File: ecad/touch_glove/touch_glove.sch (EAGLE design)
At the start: 173 parts, among them Q1 MCH3474 4A/30V, Q2 MCH3474 4A/30V, Q3 MCH3474 4A/30V, Q4 MCH3474 4A/30V, Q5 MCH3474 4A/30V, Q6 MCH3474 4A/30V, SW1 4A/28V

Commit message: Completed most of the circuitry for the ET schematic.
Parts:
- added C37, C49, C63, C64, C66, C67, C68, C69, C70, C76, C78, C80: 0.1uF/50V, _capacitors:0.1UF_SMD-0402_50V-10%
- added C61: 0.1uF/25V, _capacitors:0.1UF_SMD-0603_50V-20%
- added C62: 0.1uF/250V, _capacitors:0.1UF_SMD-0805_250V-10%
- added C65: 100uF/10V, _capacitors:100UF-POLARIZED_TANT_SMD-1206_10V-20%
- added C71, C72, C73, C75, C77, C79: 10uF/6.3V, _capacitors:10UF_CER_SMD-0402_6.3V-20%
- added C74: 4.7uF/10V/0402, _capacitors:4.7UF_CER_SMD-0402_10V-20%
- added ET_INDEX_PIXEL1-1, ET_INDEX_PIXEL1-10, ET_INDEX_PIXEL1-11, ET_INDEX_PIXEL1-12, ET_INDEX_PIXEL1-13, ET_INDEX_PIXEL1-14, ET_INDEX_PIXEL1-15, ET_INDEX_PIXEL1-16, ET_INDEX_PIXEL1-17, ET_INDEX_PIXEL1-18, ET_INDEX_PIXEL1-19, ET_INDEX_PIXEL1-2, ET_INDEX_PIXEL1-20, ET_INDEX_PIXEL1-3, ET_INDEX_PIXEL1-4, ET_INDEX_PIXEL1-5, ET_INDEX_PIXEL1-6, ET_INDEX_PIXEL1-7, ET_INDEX_PIXEL1-8, ET_INDEX_PIXEL1-9, ET_INDEX_PIXEL2-1, ET_INDEX_PIXEL2-10, ET_INDEX_PIXEL2-11, ET_INDEX_PIXEL2-12, ET_INDEX_PIXEL2-13, ET_INDEX_PIXEL2-14, ET_INDEX_PIXEL2-15, ET_INDEX_PIXEL2-16, ET_INDEX_PIXEL2-17, ET_INDEX_PIXEL2-18, ET_INDEX_PIXEL2-19, ET_INDEX_PIXEL2-2, ET_INDEX_PIXEL2-20, ET_INDEX_PIXEL2-3, ET_INDEX_PIXEL2-4, ET_INDEX_PIXEL2-5, ET_INDEX_PIXEL2-6, ET_INDEX_PIXEL2-7, ET_INDEX_PIXEL2-8, ET_INDEX_PIXEL2-9, ET_INDEX_PIXEL3-1, ET_INDEX_PIXEL3-10, ET_INDEX_PIXEL3-11, ET_INDEX_PIXEL3-12, ET_INDEX_PIXEL3-13, ET_INDEX_PIXEL3-14, ET_INDEX_PIXEL3-15, ET_INDEX_PIXEL3-16, ET_INDEX_PIXEL3-17, ET_INDEX_PIXEL3-18, ET_INDEX_PIXEL3-19, ET_INDEX_PIXEL3-2, ET_INDEX_PIXEL3-20, ET_INDEX_PIXEL3-3, ET_INDEX_PIXEL3-4, ET_INDEX_PIXEL3-5, ET_INDEX_PIXEL3-6, ET_INDEX_PIXEL3-7, ET_INDEX_PIXEL3-8, ET_INDEX_PIXEL3-9, ET_INDEX_PIXEL4-1, ET_INDEX_PIXEL4-10, ET_INDEX_PIXEL4-11, ET_INDEX_PIXEL4-12, ET_INDEX_PIXEL4-13, ET_INDEX_PIXEL4-14, ET_INDEX_PIXEL4-15, ET_INDEX_PIXEL4-16, ET_INDEX_PIXEL4-17, ET_INDEX_PIXEL4-18, ET_INDEX_PIXEL4-19, ET_INDEX_PIXEL4-2, ET_INDEX_PIXEL4-20, ET_INDEX_PIXEL4-3, ET_INDEX_PIXEL4-4, ET_INDEX_PIXEL4-5, ET_INDEX_PIXEL4-6, ET_INDEX_PIXEL4-7, ET_INDEX_PIXEL4-8, ET_INDEX_PIXEL4-9: SPST-NO 170mA 250V, _relay:RELAY_SOLID-STATE_SSR_170MA_250V_SPST-NO
- added IC1: DRV8662, _special:DRV8662_PIEZO_HAPTICS_DRIVER_QFN-20-EP
- added J1, J2, J3, J4, J5: VERT MALE 2.54MM, _connectors:1X16_PTH_VERT_MALE_2.54MM
- added J6, J7, J8, J9: PTH VERT MALE, _connectors:1X02_PTH_VERT_MALE_2.54MM
- added L3: 4.7uH/1.4A, _inductors:4.7UH_SMD-2520_1.4A-0.216OHM-20%
- added L4: 10uH/380mA, _inductors:10UH_SMD-0603_0.38A-0.468OHM-10%
- added NFET1: 2N7002DW, _transistors:MOSFET_N-CHANNEL_2-ARRAY_2N7002DW_115MA-60V
- added OPAMP4: TLV2361_GP_20MA_7MHZ, _op_amps:TLV2361_GP_20MA_7MHZ
- added POT1: 100K, _resistors:POTENTIOMETER_ST4ETB104_100K-1/4W-20%
- added PWM_DRIVER2, PWM_DRIVER3, PWM_DRIVER4, PWM_DRIVER5, PWM_DRIVER6: PCA9685, _special:PCA9685_16-CH_12-BIT_PWM-DRIVER_TSSOP-28_PWM-DRIVER_16CH
- added R100, R101, R102, R103, R104, R105, R106, R107, R108, R109, R110, R111, R112, R113, R114, R115, R116, R117, R118, R119, R120, R121, R122, R123, R124, R125, R126, R127, R128, R129, R130, R131, R132, R133, R134, R135, R49, R57, R58, R59, R60, R61, R62, R63, R64, R65, R66, R67, R68, R69, R70, R71, R72, R73, R74, R75, R76, R77, R78, R79, R80, R81, R82, R83, R84, R85, R86, R87, R88, R89, R90, R91, R92, R93, R94, R95, R96, R97, R98, R99: 1K, _resistors:1KΩ_SMD-0402_1/16W-5%
- added R136, R137, R54, R55, R56: 10K, _resistors:10KΩ_SMD-0402_1/16W-5%
- added R50: 768K, _resistors:768KΩ_SMD-0402_1/16W-1%
- added R51: 35.7K, _resistors:35.7KΩ_SMD-0402_1/16W-1%
- added R52: 20K, _resistors:20KΩ_SMD-0402_1/16W-1%
- added R53: 41.2K, _resistors:41.2KΩ_SMD-0402_1/16W-1%
- added REXT: 7.5K, _resistors:7.5KΩ_SMD-0402_1/16W-1%
- added SW2: 25mA/24V, _switches:SWITCH_SPST_ARRAY-3_SLIDE_DIP_SPST_25MA_24V
- added VREG-MCU1: TPS76833QDR 1A/3.3V, _ic_power:VREG_TPS768XX_ULDO_FAST-TRANSIENT_TPS76833QDR_1A-3.3V
- added VREG2: NCP1729 50mA, _ic_power:VREG_NCP1729_NEGATIVE_SWITCHED-CAP-INVERTER_50MA
- added VREG3: TPS62202 300mA 1.8V, _ic_power:VREG_SWITCHING_TPS6220XTPS62202_300MA_1.8V
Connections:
- new net -1.8V: C72.1, OPAMP4.V-, VREG2.VOUT
- new net C+: C71.1, VREG2.C+
- new net C-: C71.2, VREG2.C-
- new net EN: IC1.EN, R54.2, SW2.S3
- new net FB: IC1.FB, R50.1, R51.2, R52.2, R53.2
- new net GAIN0: IC1.GAIN0, NFET1.G2, R55.2, SW2.S2
- new net GAIN1: IC1.GAIN1, NFET1.G1, R56.2, SW2.S1
- new net IN+: C64.1, OPAMP4.OUT, POT1.CCW, POT1.S, R136.2
- new net INDEX_IN1-1: ET_INDEX_PIXEL1-1.1, ET_INDEX_PIXEL1-13.1, ET_INDEX_PIXEL1-17.1, ET_INDEX_PIXEL1-5.1, ET_INDEX_PIXEL1-9.1, PWM_DRIVER2.PWM0, PWM_DRIVER3.PWM0, PWM_DRIVER4.PWM0, PWM_DRIVER5.PWM0, PWM_DRIVER6.PWM0
- new net INDEX_IN1-2: ET_INDEX_PIXEL1-10.1, ET_INDEX_PIXEL1-14.1, ET_INDEX_PIXEL1-18.1, ET_INDEX_PIXEL1-2.1, ET_INDEX_PIXEL1-6.1, PWM_DRIVER2.PWM1, PWM_DRIVER3.PWM1, PWM_DRIVER4.PWM1, PWM_DRIVER5.PWM1, PWM_DRIVER6.PWM1
- new net INDEX_IN1-3: ET_INDEX_PIXEL1-11.1, ET_INDEX_PIXEL1-15.1, ET_INDEX_PIXEL1-19.1, ET_INDEX_PIXEL1-3.1, ET_INDEX_PIXEL1-7.1, PWM_DRIVER2.PWM2, PWM_DRIVER3.PWM2, PWM_DRIVER4.PWM2, PWM_DRIVER5.PWM2, PWM_DRIVER6.PWM2
- new net INDEX_IN1-4: ET_INDEX_PIXEL1-12.1, ET_INDEX_PIXEL1-16.1, ET_INDEX_PIXEL1-20.1, ET_INDEX_PIXEL1-4.1, ET_INDEX_PIXEL1-8.1, PWM_DRIVER2.PWM3, PWM_DRIVER3.PWM3, PWM_DRIVER4.PWM3, PWM_DRIVER5.PWM3, PWM_DRIVER6.PWM3
- new net INDEX_IN2-1: ET_INDEX_PIXEL2-1.1, ET_INDEX_PIXEL2-11.1, ET_INDEX_PIXEL2-15.1, ET_INDEX_PIXEL2-19.1, ET_INDEX_PIXEL2-7.1, PWM_DRIVER2.PWM4, PWM_DRIVER3.PWM4, PWM_DRIVER4.PWM4, PWM_DRIVER5.PWM4, PWM_DRIVER6.PWM4
- new net INDEX_IN2-2: ET_INDEX_PIXEL2-10.1, ET_INDEX_PIXEL2-14.1, ET_INDEX_PIXEL2-18.1, ET_INDEX_PIXEL2-2.1, ET_INDEX_PIXEL2-6.1, PWM_DRIVER2.PWM5, PWM_DRIVER3.PWM5, PWM_DRIVER4.PWM5, PWM_DRIVER5.PWM5, PWM_DRIVER6.PWM5
- new net INDEX_IN2-3: ET_INDEX_PIXEL2-13.1, ET_INDEX_PIXEL2-17.1, ET_INDEX_PIXEL2-3.1, ET_INDEX_PIXEL2-5.1, ET_INDEX_PIXEL2-9.1, PWM_DRIVER2.PWM6, PWM_DRIVER3.PWM6, PWM_DRIVER4.PWM6, PWM_DRIVER5.PWM6, PWM_DRIVER6.PWM6
- new net INDEX_IN2-4: ET_INDEX_PIXEL2-12.1, ET_INDEX_PIXEL2-16.1, ET_INDEX_PIXEL2-20.1, ET_INDEX_PIXEL2-4.1, ET_INDEX_PIXEL2-8.1, PWM_DRIVER2.PWM7, PWM_DRIVER3.PWM7, PWM_DRIVER4.PWM7, PWM_DRIVER5.PWM7, PWM_DRIVER6.PWM7
- new net INDEX_IN3-1: ET_INDEX_PIXEL3-1.1, ET_INDEX_PIXEL3-13.1, ET_INDEX_PIXEL3-17.1, ET_INDEX_PIXEL3-5.1, ET_INDEX_PIXEL3-9.1, PWM_DRIVER2.PWM8, PWM_DRIVER3.PWM8, PWM_DRIVER4.PWM8, PWM_DRIVER5.PWM8, PWM_DRIVER6.PWM8
- new net INDEX_IN3-2: ET_INDEX_PIXEL3-10.1, ET_INDEX_PIXEL3-14.1, ET_INDEX_PIXEL3-18.1, ET_INDEX_PIXEL3-2.1, ET_INDEX_PIXEL3-6.1, PWM_DRIVER2.PWM9, PWM_DRIVER3.PWM9, PWM_DRIVER4.PWM9, PWM_DRIVER5.PWM9, PWM_DRIVER6.PWM9
- new net INDEX_IN3-3: ET_INDEX_PIXEL3-11.1, ET_INDEX_PIXEL3-15.1, ET_INDEX_PIXEL3-19.1, ET_INDEX_PIXEL3-3.1, ET_INDEX_PIXEL3-7.1, PWM_DRIVER2.PWM10, PWM_DRIVER3.PWM10, PWM_DRIVER4.PWM10, PWM_DRIVER5.PWM10, PWM_DRIVER6.PWM10
- new net INDEX_IN3-4: ET_INDEX_PIXEL3-12.1, ET_INDEX_PIXEL3-16.1, ET_INDEX_PIXEL3-20.1, ET_INDEX_PIXEL3-4.1, ET_INDEX_PIXEL3-8.1, PWM_DRIVER2.PWM11, PWM_DRIVER3.PWM11, PWM_DRIVER4.PWM11, PWM_DRIVER5.PWM11, PWM_DRIVER6.PWM11
- new net INDEX_IN4-1: ET_INDEX_PIXEL4-1.1, ET_INDEX_PIXEL4-13.1, ET_INDEX_PIXEL4-17.1, ET_INDEX_PIXEL4-5.1, ET_INDEX_PIXEL4-9.1, PWM_DRIVER2.PWM12, PWM_DRIVER3.PWM12, PWM_DRIVER4.PWM12, PWM_DRIVER5.PWM12, PWM_DRIVER6.PWM12
- new net INDEX_IN4-2: ET_INDEX_PIXEL4-10.1, ET_INDEX_PIXEL4-14.1, ET_INDEX_PIXEL4-18.1, ET_INDEX_PIXEL4-2.1, ET_INDEX_PIXEL4-6.1, PWM_DRIVER2.PWM13, PWM_DRIVER3.PWM13, PWM_DRIVER4.PWM13, PWM_DRIVER5.PWM13, PWM_DRIVER6.PWM13
- new net INDEX_IN4-3: ET_INDEX_PIXEL4-11.1, ET_INDEX_PIXEL4-15.1, ET_INDEX_PIXEL4-19.1, ET_INDEX_PIXEL4-3.1, ET_INDEX_PIXEL4-7.1, PWM_DRIVER2.PWM14, PWM_DRIVER3.PWM14, PWM_DRIVER4.PWM14, PWM_DRIVER5.PWM14, PWM_DRIVER6.PWM14
- new net INDEX_IN4-4: ET_INDEX_PIXEL4-12.1, ET_INDEX_PIXEL4-16.1, ET_INDEX_PIXEL4-20.1, ET_INDEX_PIXEL4-4.1, ET_INDEX_PIXEL4-8.1, PWM_DRIVER2.PWM15, PWM_DRIVER3.PWM15, PWM_DRIVER4.PWM15, PWM_DRIVER5.PWM15, PWM_DRIVER6.PWM15
- new net INDEX_OUT1-1: ET_INDEX_PIXEL1-1.3, ET_INDEX_PIXEL1-13.3, ET_INDEX_PIXEL1-17.3, ET_INDEX_PIXEL1-5.3, ET_INDEX_PIXEL1-9.3, J1.1, J2.1, J3.1, J4.1, J5.1
- new net INDEX_OUT1-2: ET_INDEX_PIXEL1-10.3, ET_INDEX_PIXEL1-14.3, ET_INDEX_PIXEL1-18.3, ET_INDEX_PIXEL1-2.3, ET_INDEX_PIXEL1-6.3
- new net INDEX_OUT1-3: ET_INDEX_PIXEL1-11.3, ET_INDEX_PIXEL1-15.3, ET_INDEX_PIXEL1-19.3, ET_INDEX_PIXEL1-3.3, ET_INDEX_PIXEL1-7.3
- new net INDEX_OUT1-4: ET_INDEX_PIXEL1-12.3, ET_INDEX_PIXEL1-16.3, ET_INDEX_PIXEL1-20.3, ET_INDEX_PIXEL1-4.3, ET_INDEX_PIXEL1-8.3
- new net INDEX_OUT2-1: ET_INDEX_PIXEL2-1.3, ET_INDEX_PIXEL2-11.3, ET_INDEX_PIXEL2-15.3, ET_INDEX_PIXEL2-19.3, ET_INDEX_PIXEL2-7.3
- new net INDEX_OUT2-2: ET_INDEX_PIXEL2-10.3, ET_INDEX_PIXEL2-14.3, ET_INDEX_PIXEL2-18.3, ET_INDEX_PIXEL2-2.3, ET_INDEX_PIXEL2-6.3
- new net INDEX_OUT2-3: ET_INDEX_PIXEL2-13.3, ET_INDEX_PIXEL2-17.3, ET_INDEX_PIXEL2-3.3, ET_INDEX_PIXEL2-5.3, ET_INDEX_PIXEL2-9.3
- new net INDEX_OUT2-4: ET_INDEX_PIXEL2-12.3, ET_INDEX_PIXEL2-16.3, ET_INDEX_PIXEL2-20.3, ET_INDEX_PIXEL2-4.3, ET_INDEX_PIXEL2-8.3
- new net INDEX_OUT3-1: ET_INDEX_PIXEL3-1.3, ET_INDEX_PIXEL3-13.3, ET_INDEX_PIXEL3-17.3, ET_INDEX_PIXEL3-5.3, ET_INDEX_PIXEL3-9.3
- new net INDEX_OUT3-2: ET_INDEX_PIXEL3-10.3, ET_INDEX_PIXEL3-14.3, ET_INDEX_PIXEL3-18.3, ET_INDEX_PIXEL3-2.3, ET_INDEX_PIXEL3-6.3
- new net INDEX_OUT3-3: ET_INDEX_PIXEL3-11.3, ET_INDEX_PIXEL3-15.3, ET_INDEX_PIXEL3-19.3, ET_INDEX_PIXEL3-3.3, ET_INDEX_PIXEL3-7.3
- new net INDEX_OUT3-4: ET_INDEX_PIXEL3-12.3, ET_INDEX_PIXEL3-16.3, ET_INDEX_PIXEL3-20.3, ET_INDEX_PIXEL3-4.3, ET_INDEX_PIXEL3-8.3
- new net INDEX_OUT4-1: ET_INDEX_PIXEL4-1.3, ET_INDEX_PIXEL4-13.3, ET_INDEX_PIXEL4-17.3, ET_INDEX_PIXEL4-5.3, ET_INDEX_PIXEL4-9.3
- new net INDEX_OUT4-2: ET_INDEX_PIXEL4-10.3, ET_INDEX_PIXEL4-14.3, ET_INDEX_PIXEL4-18.3, ET_INDEX_PIXEL4-2.3, ET_INDEX_PIXEL4-6.3
- new net INDEX_OUT4-3: ET_INDEX_PIXEL4-11.3, ET_INDEX_PIXEL4-15.3, ET_INDEX_PIXEL4-19.3, ET_INDEX_PIXEL4-3.3, ET_INDEX_PIXEL4-7.3
- new net INDEX_OUT4-4: ET_INDEX_PIXEL4-12.3, ET_INDEX_PIXEL4-16.3, ET_INDEX_PIXEL4-20.3, ET_INDEX_PIXEL4-4.3, ET_INDEX_PIXEL4-8.3
- new net N$100: ET_INDEX_PIXEL3-12.2, R99.2
- new net N$101: ET_INDEX_PIXEL4-9.2, R100.2
- new net N$102: ET_INDEX_PIXEL4-10.2, R101.2
- new net N$103: ET_INDEX_PIXEL4-11.2, R102.2
- new net N$104: ET_INDEX_PIXEL4-12.2, R103.2
- new net N$105: ET_INDEX_PIXEL1-13.2, R104.2
- new net N$106: ET_INDEX_PIXEL1-14.2, R105.2
- new net N$107: ET_INDEX_PIXEL1-15.2, R106.2
- new net N$108: ET_INDEX_PIXEL1-16.2, R107.2
- new net N$109: ET_INDEX_PIXEL2-15.2, R108.2
- new net N$110: ET_INDEX_PIXEL2-14.2, R109.2
- new net N$111: ET_INDEX_PIXEL2-13.2, R110.2
- new net N$112: ET_INDEX_PIXEL2-16.2, R111.2
- new net N$113: ET_INDEX_PIXEL3-13.2, R112.2
- new net N$114: ET_INDEX_PIXEL3-14.2, R113.2
- new net N$115: ET_INDEX_PIXEL3-15.2, R114.2
- new net N$116: ET_INDEX_PIXEL3-16.2, R115.2
- new net N$117: ET_INDEX_PIXEL4-13.2, R116.2
- new net N$118: ET_INDEX_PIXEL4-14.2, R117.2
- new net N$119: ET_INDEX_PIXEL4-15.2, R118.2
- new net N$120: ET_INDEX_PIXEL4-16.2, R119.2
- new net N$121: ET_INDEX_PIXEL1-17.2, R120.2
- new net N$122: ET_INDEX_PIXEL1-18.2, R121.2
- new net N$123: ET_INDEX_PIXEL1-19.2, R122.2
- new net N$124: ET_INDEX_PIXEL1-20.2, R123.2
- new net N$125: ET_INDEX_PIXEL2-19.2, R124.2
- new net N$126: ET_INDEX_PIXEL2-18.2, R125.2
- new net N$127: ET_INDEX_PIXEL2-17.2, R126.2
- new net N$128: ET_INDEX_PIXEL2-20.2, R127.2
- new net N$129: ET_INDEX_PIXEL3-17.2, R128.2
- new net N$130: ET_INDEX_PIXEL3-18.2, R129.2
- new net N$131: ET_INDEX_PIXEL3-19.2, R130.2
- new net N$132: ET_INDEX_PIXEL3-20.2, R131.2
- new net N$133: ET_INDEX_PIXEL4-17.2, R132.2
- new net N$134: ET_INDEX_PIXEL4-18.2, R133.2
- new net N$135: ET_INDEX_PIXEL4-19.2, R134.2
- new net N$136: ET_INDEX_PIXEL4-20.2, R135.2
- new net N$137: L4.1, VREG3.VOUT
- new net N$138: OPAMP4.IN+, R136.1, R137.2
- new net N$139: C76.1, OPAMP4.IN-, POT1.CW
- new net N$33: ET_INDEX_PIXEL1-3.2, R58.2
- new net N$39: ET_INDEX_PIXEL1-1.2, R49.2
- new net N$42: IC1.SW, L3.1
- new net N$43: C49.1, IC1.VPUMP
- new net N$44: C62.1, IC1.PVDD, IC1.VBST, R50.2
- new net N$48: IC1.REXT, REXT.2
- new net N$49: NFET1.D1, R52.1
- new net N$51: NFET1.D2, R53.1
- new net N$52: C64.2, IC1.IN+
- new net N$56: C63.2, IC1.IN-
- new net N$57: ET_INDEX_PIXEL1-2.2, R57.2
- new net N$58: ET_INDEX_PIXEL1-5.2, R72.2
- new net N$59: ET_INDEX_PIXEL1-4.2, R59.2
- new net N$60: ET_INDEX_PIXEL2-1.2, R60.2
- new net N$61: ET_INDEX_PIXEL2-2.2, R61.2
- new net N$64: ET_INDEX_PIXEL2-3.2, R62.2
- new net N$65: ET_INDEX_PIXEL2-4.2, R63.2
- new net N$66: ET_INDEX_PIXEL3-1.2, R64.2
- new net N$67: ET_INDEX_PIXEL3-2.2, R65.2
- new net N$68: ET_INDEX_PIXEL3-3.2, R66.2
- new net N$69: ET_INDEX_PIXEL3-4.2, R67.2
- new net N$70: ET_INDEX_PIXEL4-1.2, R68.2
- new net N$71: ET_INDEX_PIXEL4-2.2, R69.2
- new net N$72: ET_INDEX_PIXEL4-3.2, R70.2
- new net N$73: ET_INDEX_PIXEL4-4.2, R71.2
- new net N$74: ET_INDEX_PIXEL1-6.2, R73.2
- new net N$75: ET_INDEX_PIXEL1-7.2, R74.2
- new net N$76: ET_INDEX_PIXEL1-8.2, R75.2
- new net N$77: ET_INDEX_PIXEL2-7.2, R76.2
- new net N$78: ET_INDEX_PIXEL2-6.2, R77.2
- new net N$79: ET_INDEX_PIXEL2-5.2, R78.2
- new net N$80: ET_INDEX_PIXEL2-8.2, R79.2
- new net N$81: ET_INDEX_PIXEL3-5.2, R80.2
- new net N$82: ET_INDEX_PIXEL3-6.2, R81.2
- new net N$83: ET_INDEX_PIXEL3-7.2, R82.2
- new net N$84: ET_INDEX_PIXEL3-8.2, R83.2
- new net N$85: ET_INDEX_PIXEL4-5.2, R84.2
- new net N$86: ET_INDEX_PIXEL4-6.2, R85.2
- new net N$87: ET_INDEX_PIXEL4-7.2, R86.2
- new net N$88: ET_INDEX_PIXEL4-8.2, R87.2
- new net N$89: ET_INDEX_PIXEL1-9.2, R88.2
- new net N$90: ET_INDEX_PIXEL1-10.2, R89.2
- new net N$91: ET_INDEX_PIXEL1-11.2, R90.2
- new net N$92: ET_INDEX_PIXEL1-12.2, R91.2
- new net N$93: ET_INDEX_PIXEL2-11.2, R92.2
- new net N$94: ET_INDEX_PIXEL2-10.2, R93.2
- new net N$95: ET_INDEX_PIXEL2-9.2, R94.2
- new net N$96: ET_INDEX_PIXEL2-12.2, R95.2
- new net N$97: ET_INDEX_PIXEL3-9.2, R96.2
- new net N$98: ET_INDEX_PIXEL3-10.2, R97.2
- new net N$99: ET_INDEX_PIXEL3-11.2, R98.2
- new net V+: ET_INDEX_PIXEL1-1.4, ET_INDEX_PIXEL1-10.4, ET_INDEX_PIXEL1-11.4, ET_INDEX_PIXEL1-12.4, ET_INDEX_PIXEL1-13.4, ET_INDEX_PIXEL1-14.4, ET_INDEX_PIXEL1-15.4, ET_INDEX_PIXEL1-16.4, ET_INDEX_PIXEL1-17.4, ET_INDEX_PIXEL1-18.4, ET_INDEX_PIXEL1-19.4, ET_INDEX_PIXEL1-2.4, ET_INDEX_PIXEL1-20.4, ET_INDEX_PIXEL1-3.4, ET_INDEX_PIXEL1-4.4, ET_INDEX_PIXEL1-5.4, ET_INDEX_PIXEL1-6.4, ET_INDEX_PIXEL1-7.4, ET_INDEX_PIXEL1-8.4, ET_INDEX_PIXEL1-9.4, ET_INDEX_PIXEL2-1.4, ET_INDEX_PIXEL2-10.4, ET_INDEX_PIXEL2-11.4, ET_INDEX_PIXEL2-12.4, ET_INDEX_PIXEL2-13.4, ET_INDEX_PIXEL2-14.4, ET_INDEX_PIXEL2-15.4, ET_INDEX_PIXEL2-16.4, ET_INDEX_PIXEL2-17.4, ET_INDEX_PIXEL2-18.4, ET_INDEX_PIXEL2-19.4, ET_INDEX_PIXEL2-2.4, ET_INDEX_PIXEL2-20.4, ET_INDEX_PIXEL2-3.4, ET_INDEX_PIXEL2-4.4, ET_INDEX_PIXEL2-5.4, ET_INDEX_PIXEL2-6.4, ET_INDEX_PIXEL2-7.4, ET_INDEX_PIXEL2-8.4, ET_INDEX_PIXEL2-9.4, ET_INDEX_PIXEL3-1.4, ET_INDEX_PIXEL3-10.4, ET_INDEX_PIXEL3-11.4, ET_INDEX_PIXEL3-12.4, ET_INDEX_PIXEL3-13.4, ET_INDEX_PIXEL3-14.4, ET_INDEX_PIXEL3-15.4, ET_INDEX_PIXEL3-16.4, ET_INDEX_PIXEL3-17.4, ET_INDEX_PIXEL3-18.4, ET_INDEX_PIXEL3-19.4, ET_INDEX_PIXEL3-2.4, ET_INDEX_PIXEL3-20.4, ET_INDEX_PIXEL3-3.4, ET_INDEX_PIXEL3-4.4, ET_INDEX_PIXEL3-5.4, ET_INDEX_PIXEL3-6.4, ET_INDEX_PIXEL3-7.4, ET_INDEX_PIXEL3-8.4, ET_INDEX_PIXEL3-9.4, ET_INDEX_PIXEL4-1.4, ET_INDEX_PIXEL4-10.4, ET_INDEX_PIXEL4-11.4, ET_INDEX_PIXEL4-12.4, ET_INDEX_PIXEL4-13.4, ET_INDEX_PIXEL4-14.4, ET_INDEX_PIXEL4-15.4, ET_INDEX_PIXEL4-16.4, ET_INDEX_PIXEL4-17.4, ET_INDEX_PIXEL4-18.4, ET_INDEX_PIXEL4-19.4, ET_INDEX_PIXEL4-2.4, ET_INDEX_PIXEL4-20.4, ET_INDEX_PIXEL4-3.4, ET_INDEX_PIXEL4-4.4, ET_INDEX_PIXEL4-5.4, ET_INDEX_PIXEL4-6.4, ET_INDEX_PIXEL4-7.4, ET_INDEX_PIXEL4-8.4, ET_INDEX_PIXEL4-9.4, IC1.OUT+
- new net V-: IC1.OUT-, J1.16, J2.16, J3.16, J4.16, J5.16
- net 1.8V: now also C73.1, C75.1, L4.2, OPAMP4.V+, VREG2.!SHDN, VREG2.VIN, VREG3.NC/FB
- net 3.3V: now also C37.1, C61.1, C65.A, C74.1, C77.1, C78.1, IC1.VDD, L3.2, SW2.P1, SW2.P2, SW2.P3, VREG-MCU1.VOUT, VREG3.VIN
- net GND: now also C37.2, C49.2, C61.2, C62.2, C63.1, C65.K, C66.2, C67.2, C68.2, C69.2, C70.2, C72.2, C73.2, C74.2, C75.2, C76.2, C77.2, C78.2, C79.2, C80.2, IC1.GND, NFET1.S1, NFET1.S2, PWM_DRIVER2.!OE, PWM_DRIVER2.A0, PWM_DRIVER2.A1, PWM_DRIVER2.A2, PWM_DRIVER2.A3, PWM_DRIVER2.A4, PWM_DRIVER2.A5, PWM_DRIVER2.EXTCLK, PWM_DRIVER2.GND, PWM_DRIVER3.!OE, PWM_DRIVER3.A0, PWM_DRIVER3.A1, PWM_DRIVER3.A2, PWM_DRIVER3.A3, PWM_DRIVER3.A4, PWM_DRIVER3.A5, PWM_DRIVER3.EXTCLK, PWM_DRIVER3.GND, PWM_DRIVER4.!OE, PWM_DRIVER4.A0, PWM_DRIVER4.A1, PWM_DRIVER4.A2, PWM_DRIVER4.A3, PWM_DRIVER4.A4, PWM_DRIVER4.A5, PWM_DRIVER4.EXTCLK, PWM_DRIVER4.GND, PWM_DRIVER5.!OE, PWM_DRIVER5.A0, PWM_DRIVER5.A1, PWM_DRIVER5.A2, PWM_DRIVER5.A3, PWM_DRIVER5.A4, PWM_DRIVER5.A5, PWM_DRIVER5.EXTCLK, PWM_DRIVER5.GND, PWM_DRIVER6.!OE, PWM_DRIVER6.A0, PWM_DRIVER6.A1, PWM_DRIVER6.A2, PWM_DRIVER6.A3, PWM_DRIVER6.A4, PWM_DRIVER6.A5, PWM_DRIVER6.EXTCLK, PWM_DRIVER6.GND, R100.1, R101.1, R102.1, R103.1, R104.1, R105.1, R106.1, R107.1, R108.1, R109.1, R110.1, R111.1, R112.1, R113.1, R114.1, R115.1, R116.1, R117.1, R118.1, R119.1, R120.1, R121.1, R122.1, R123.1, R124.1, R125.1, R126.1, R127.1, R128.1, R129.1, R130.1, R131.1, R132.1, R133.1, R134.1, R135.1, R137.1, R49.1, R51.1, R54.1, R55.1, R56.1, R57.1, R58.1, R59.1, R60.1, R61.1, R62.1, R63.1, R64.1, R65.1, R66.1, R67.1, R68.1, R69.1, R70.1, R71.1, R72.1, R73.1, R74.1, R75.1, R76.1, R77.1, R78.1, R79.1, R80.1, R81.1, R82.1, R83.1, R84.1, R85.1, R86.1, R87.1, R88.1, R89.1, R90.1, R91.1, R92.1, R93.1, R94.1, R95.1, R96.1, R97.1, R98.1, R99.1, REXT.1, VREG-MCU1.!EN, VREG-MCU1.GND, VREG2.GND, VREG3.GND
- net N$7: now also VREG3.EN
- net SCL: now also PWM_DRIVER2.SCL, PWM_DRIVER3.SCL, PWM_DRIVER4.SCL, PWM_DRIVER5.SCL, PWM_DRIVER6.SCL
- net SDA: now also PWM_DRIVER2.SDA, PWM_DRIVER3.SDA, PWM_DRIVER4.SDA, PWM_DRIVER5.SDA, PWM_DRIVER6.SDA
- net VBAT: now also C79.1, C80.1, VREG-MCU1.VIN
- net VCC: now also C66.1, C67.1, C68.1, C69.1, C70.1, PWM_DRIVER2.VCC, PWM_DRIVER3.VCC, PWM_DRIVER4.VCC, PWM_DRIVER5.VCC, PWM_DRIVER6.VCC
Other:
- note added: "ANALOG VOLTAGE AMPLIFIER"
- note added: "ELECTROTACTILE ARRAYS"
- note added: "ET ARRAY - INDEX"
- note added: "ET ARRAY - MIDDLE"
- note added: "ET ARRAY - PINKY"
- note added: "ET ARRAY - RING"
- note added: "ET ARRAY - THUMB"
- note added: "SQW GENERATOR"
- note added: "STAGE1"
- note added: "STAGE2"
- note added: "STAGE3"
- note added: "TODO: CHECK VALUES (C1, POT1, R2,R3) AND VOLTAGE DIVIDER TO MAKE 1.8V"
- note added: "TODO: Change I2C addr"
- note added: "TODO: NAME ENABLE PIN"
- note added: "Transfer: VBAT, SDA, SCL, GND"

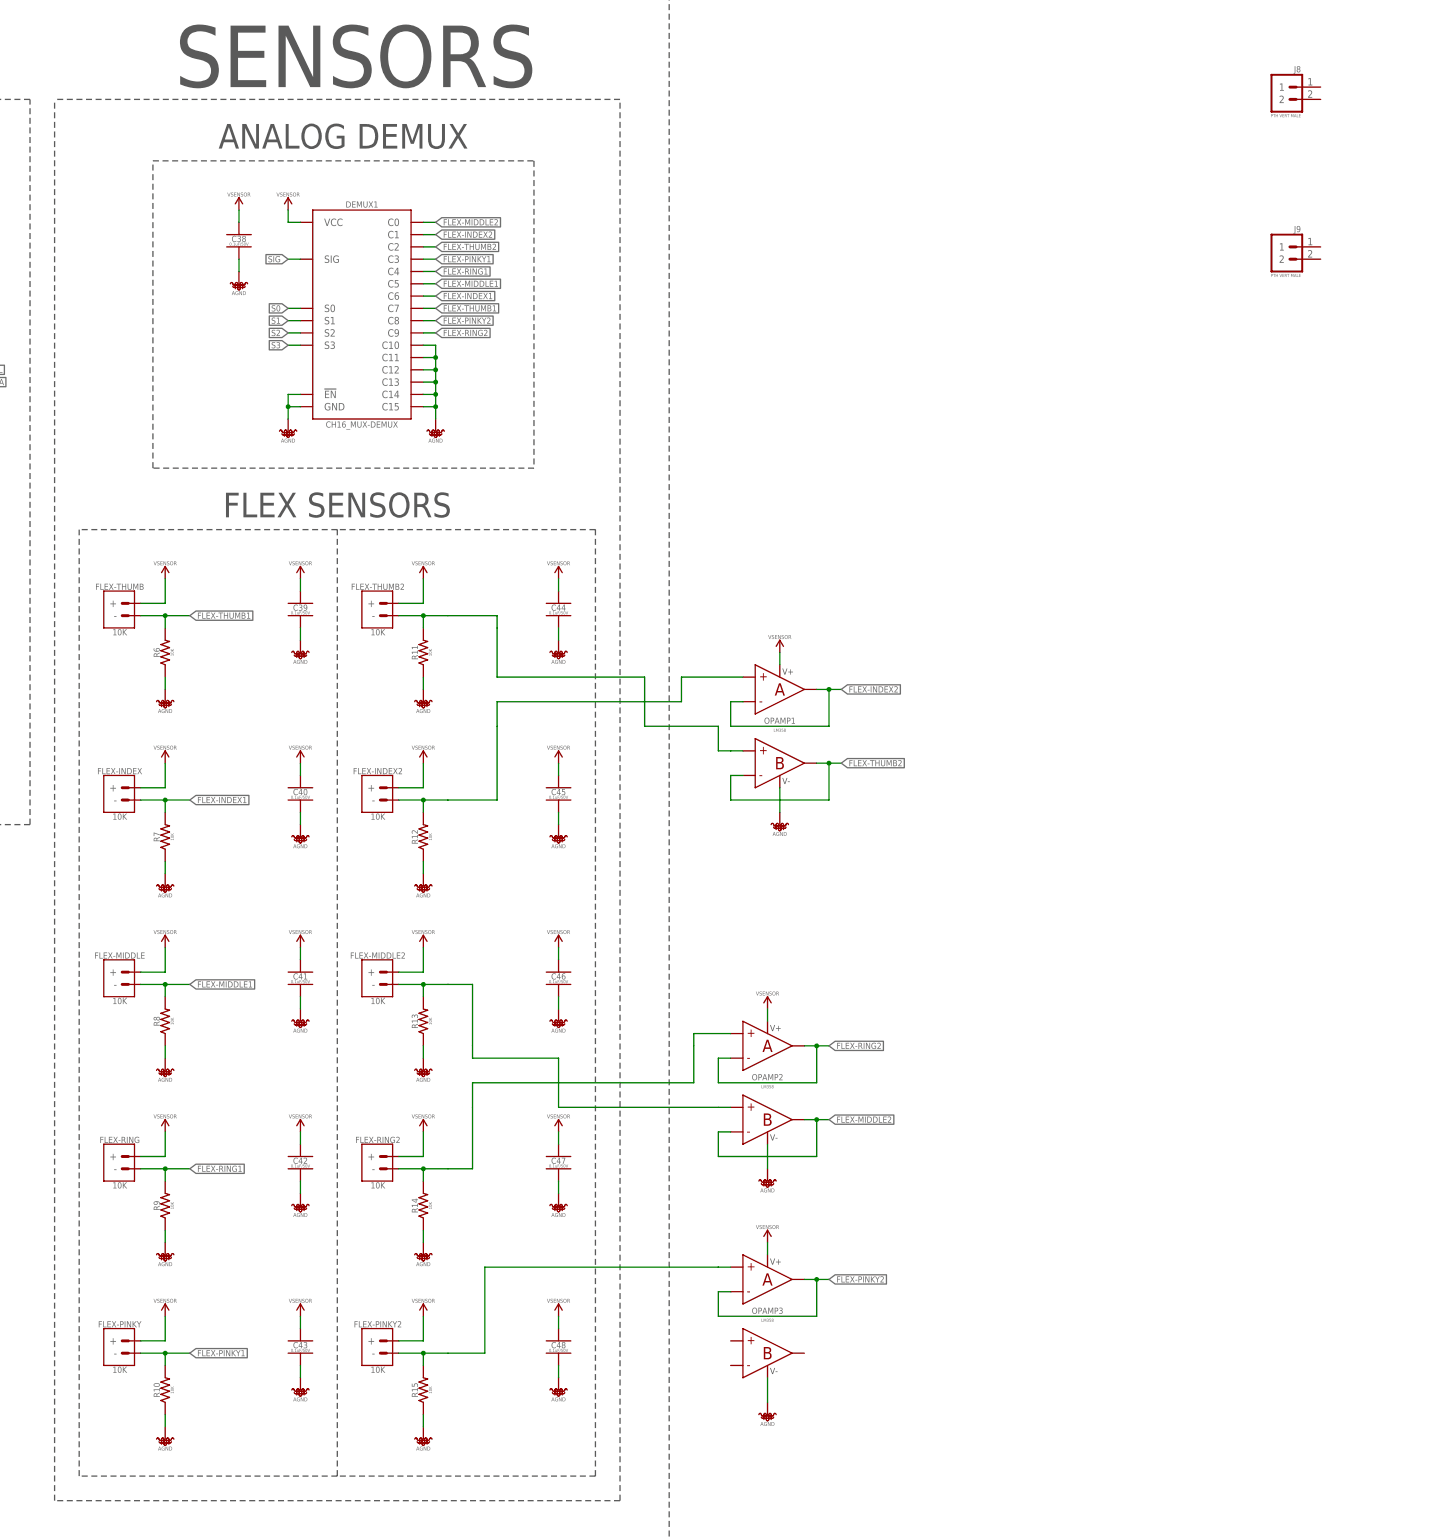
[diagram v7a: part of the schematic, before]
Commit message: Removed the 5 extra flex sensors.  Added the 4 headers that will connect to the ET extension board.
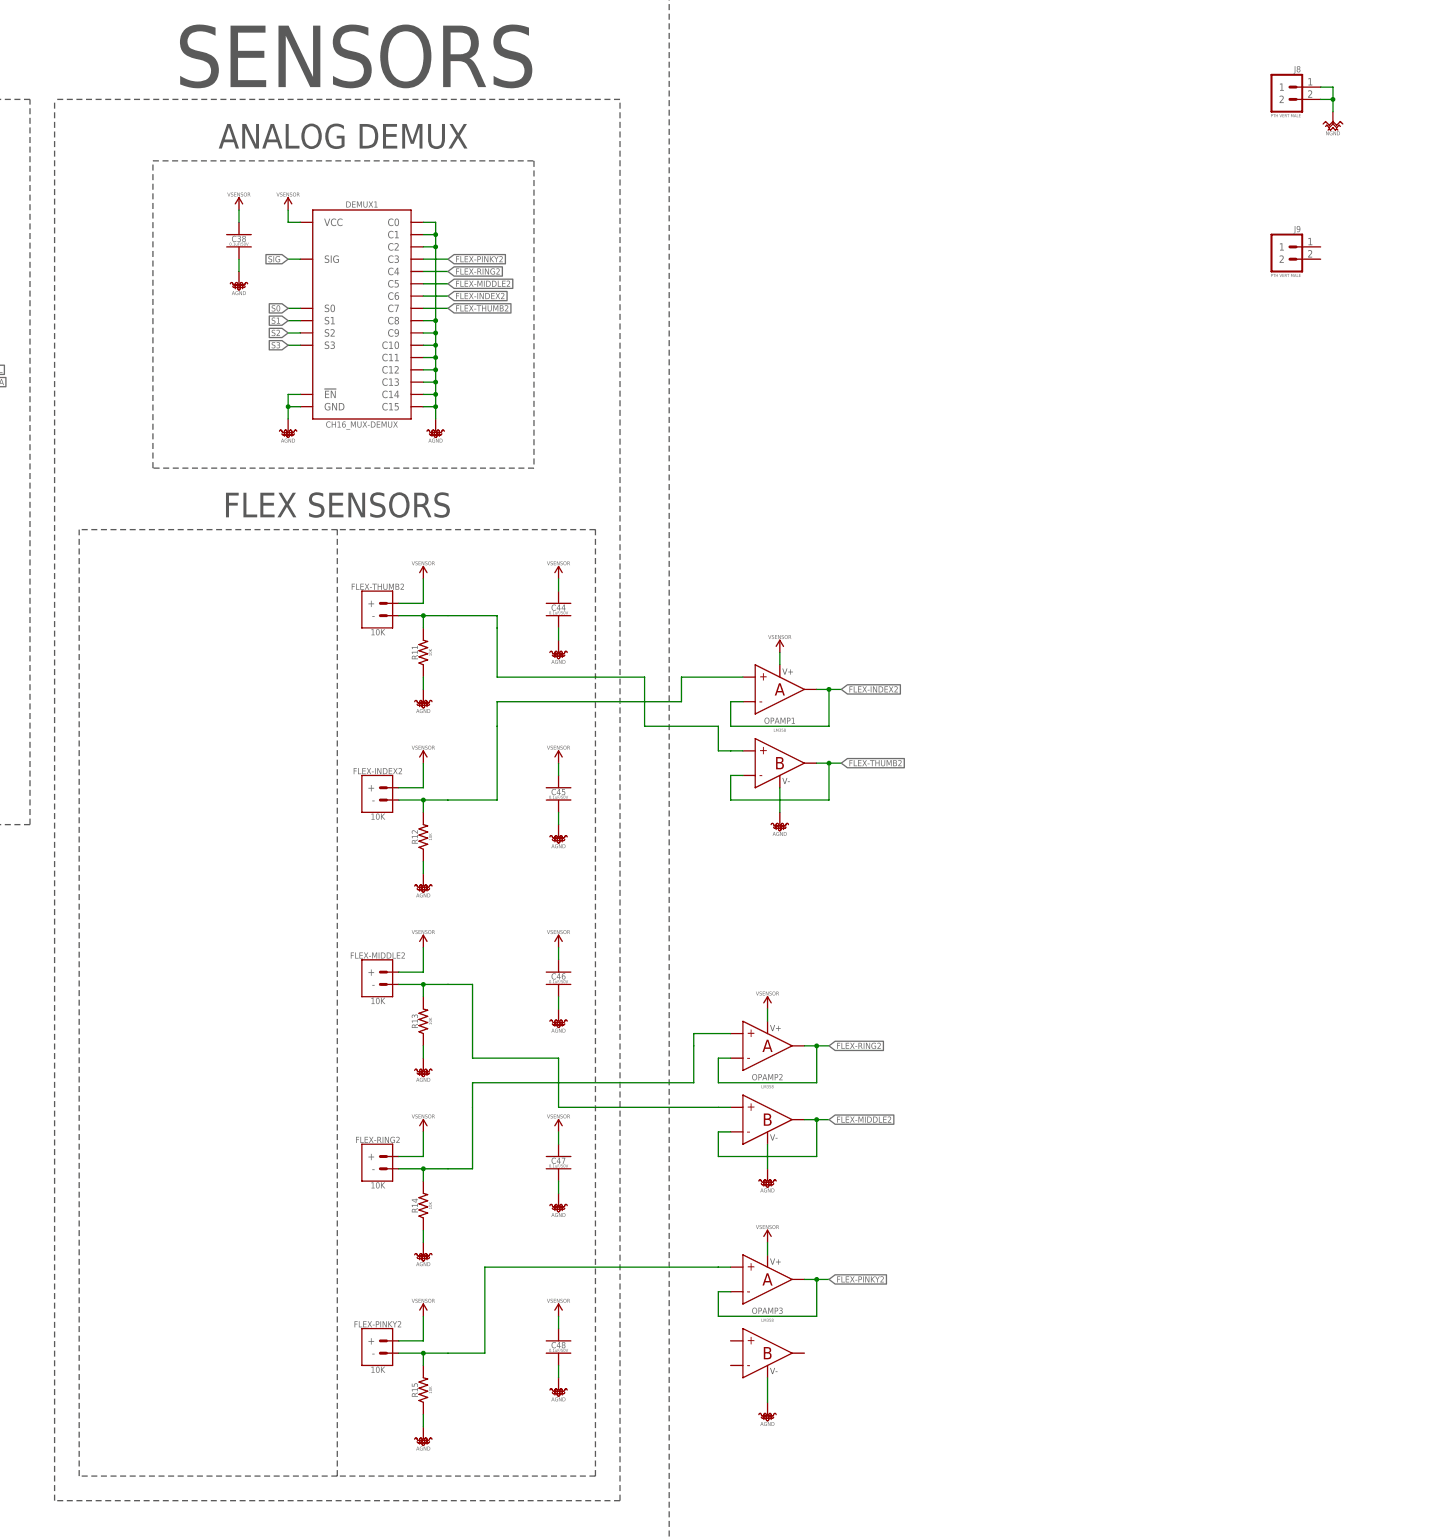
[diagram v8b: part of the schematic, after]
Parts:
- removed C39, C40, C41, C42, C43: 0.1uF/50V, _capacitors:0.1UF_SMD-0402_50V-10%
- removed FLEX-INDEX, FLEX-MIDDLE, FLEX-PINKY, FLEX-RING, FLEX-THUMB: 10K, _sensors:FLEX_SENSOR_0530470210_VERT-MALE_PITCH-1.25MM
- removed R10, R6, R7, R8, R9: 10K, _resistors:10KΩ_SMD-0402_1/16W-5%
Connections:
- removed net FLEX-INDEX1: DEMUX1.C6, FLEX-INDEX.-, R7.2
- removed net FLEX-MIDDLE1: DEMUX1.C5, FLEX-MIDDLE.-, R8.2
- removed net FLEX-PINKY1: DEMUX1.C3, FLEX-PINKY.-, R10.2
- removed net FLEX-RING1: DEMUX1.C4, FLEX-RING.-, R9.2
- removed net FLEX-THUMB1: DEMUX1.C7, FLEX-THUMB.-, R6.2
- net AGND: now also DEMUX1.C0, DEMUX1.C1, DEMUX1.C2, DEMUX1.C8, DEMUX1.C9; no longer C39.2, C40.2, C41.2, C42.2, C43.2, R10.1, R6.1, R7.1, R8.1, R9.1
- net FLEX-INDEX2: now also DEMUX1.C6; no longer DEMUX1.C1
- net FLEX-MIDDLE2: now also DEMUX1.C5; no longer DEMUX1.C0
- net FLEX-PINKY2: now also DEMUX1.C3; no longer DEMUX1.C8
- net FLEX-RING2: now also DEMUX1.C4; no longer DEMUX1.C9
- net FLEX-THUMB2: now also DEMUX1.C7; no longer DEMUX1.C2
- net NGND: now also J8.1, J8.2
- net VSENSOR: no longer C39.1, C40.1, C41.1, C42.1, C43.1, FLEX-INDEX.+, FLEX-MIDDLE.+, FLEX-PINKY.+, FLEX-RING.+, FLEX-THUMB.+
